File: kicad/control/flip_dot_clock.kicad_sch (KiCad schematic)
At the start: 33 parts, among them U1 NUCLEO-F303K8-HEADER, U10 Small_7_Seg_FlipDot_Module, U2 SLC03B-05, U3 NCV7719, U4 Small_7_Seg_FlipDot_Module, U5 NCV7719, U6 Small_7_Seg_FlipDot_Module, U7 NCV7719, U8 Small_7_Seg_FlipDot_Module, U9 NCV7719

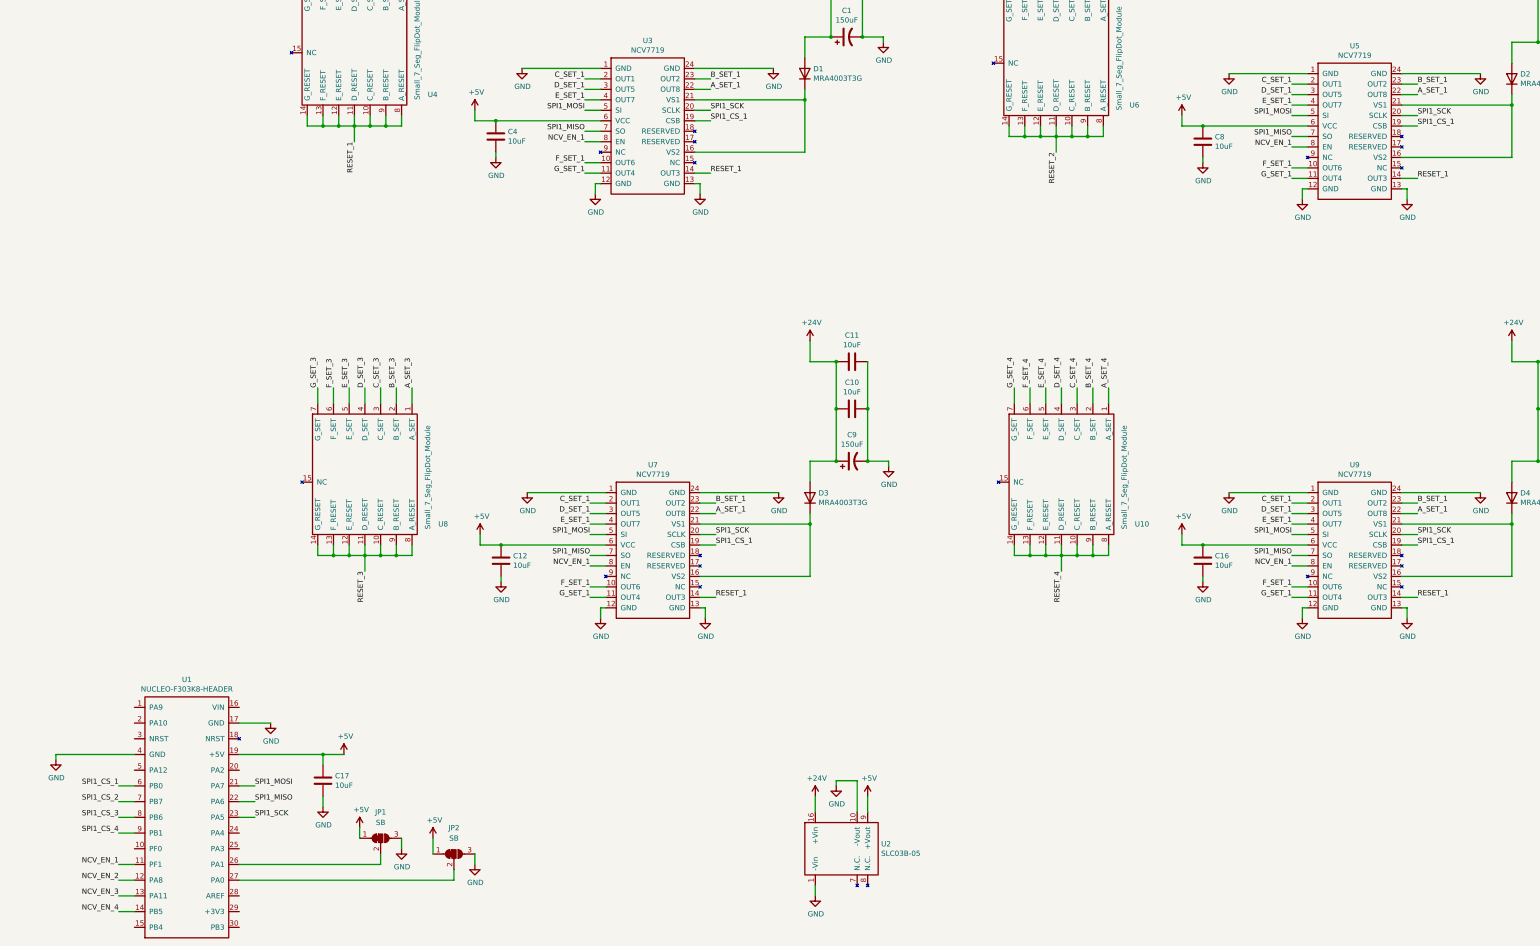
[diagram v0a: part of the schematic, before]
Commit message: all PCB nets connected
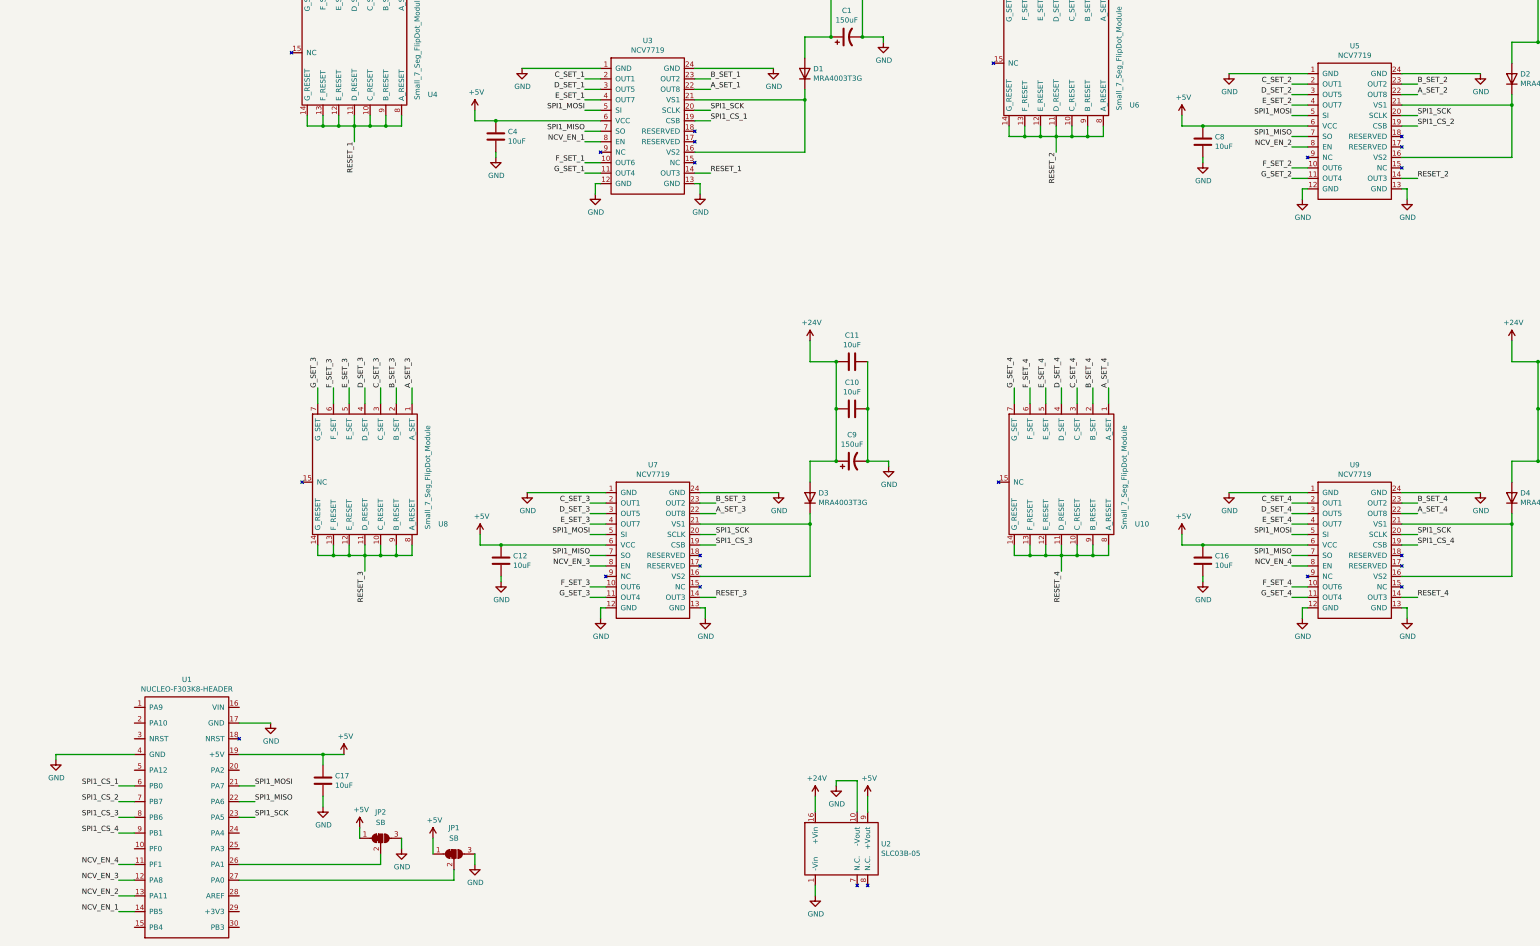
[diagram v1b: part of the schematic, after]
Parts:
- renumbered JP2 to JP1, JP1 to JP2
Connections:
- net A_SET_1: no longer U5.22 (OUT8), U7.22 (OUT8), U9.22 (OUT8)
- net A_SET_2: now also U5.22 (OUT8)
- net A_SET_3: now also U7.22 (OUT8)
- net A_SET_4: now also U9.22 (OUT8)
- net B_SET_1: no longer U5.23 (OUT2), U7.23 (OUT2), U9.23 (OUT2)
- net B_SET_2: now also U5.23 (OUT2)
- net B_SET_3: now also U7.23 (OUT2)
- net B_SET_4: now also U9.23 (OUT2)
- net C_SET_1: no longer U5.2 (OUT1), U7.2 (OUT1), U9.2 (OUT1)
- net C_SET_2: now also U5.2 (OUT1)
- net C_SET_3: now also U7.2 (OUT1)
- net C_SET_4: now also U9.2 (OUT1)
- net D_SET_1: no longer U5.3 (OUT5), U7.3 (OUT5), U9.3 (OUT5)
- net D_SET_2: now also U5.3 (OUT5)
- net D_SET_3: now also U7.3 (OUT5)
- net D_SET_4: now also U9.3 (OUT5)
- net E_SET_1: no longer U5.4 (OUT7), U7.4 (OUT7), U9.4 (OUT7)
- net E_SET_2: now also U5.4 (OUT7)
- net E_SET_3: now also U7.4 (OUT7)
- net E_SET_4: now also U9.4 (OUT7)
- net F_SET_1: no longer U5.10 (OUT6), U7.10 (OUT6), U9.10 (OUT6)
- net F_SET_2: now also U5.10 (OUT6)
- net F_SET_3: now also U7.10 (OUT6)
- net F_SET_4: now also U9.10 (OUT6)
- net G_SET_1: no longer U5.11 (OUT4), U7.11 (OUT4), U9.11 (OUT4)
- net G_SET_2: now also U5.11 (OUT4)
- net G_SET_3: now also U7.11 (OUT4)
- net G_SET_4: now also U9.11 (OUT4)
- net NCV_EN_1: now also U1.14 (PB5); no longer U1.11 (PF1), U5.8 (EN), U7.8 (EN), U9.8 (EN)
- net NCV_EN_2: now also U1.13 (PA11), U5.8 (EN); no longer U1.12 (PA8)
- net NCV_EN_3: now also U1.12 (PA8), U7.8 (EN); no longer U1.13 (PA11)
- net NCV_EN_4: now also U1.11 (PF1), U9.8 (EN); no longer U1.14 (PB5)
- net RESET_1: no longer U5.14 (OUT3), U7.14 (OUT3), U9.14 (OUT3)
- net RESET_2: now also U5.14 (OUT3)
- net RESET_3: now also U7.14 (OUT3)
- net RESET_4: now also U9.14 (OUT3)
- net SPI1_CS_1: no longer U5.19 (CSB), U7.19 (CSB), U9.19 (CSB)
- net SPI1_CS_2: now also U5.19 (CSB)
- net SPI1_CS_3: now also U7.19 (CSB)
- net SPI1_CS_4: now also U9.19 (CSB)

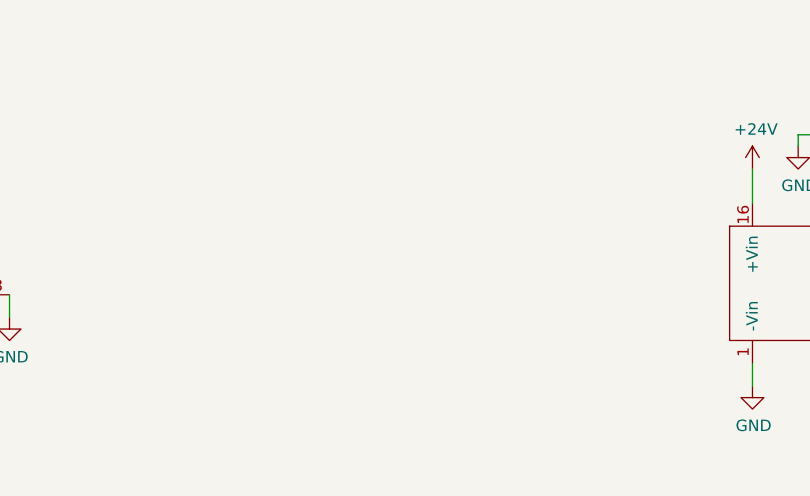
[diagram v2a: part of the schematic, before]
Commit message: update layout, add power connector
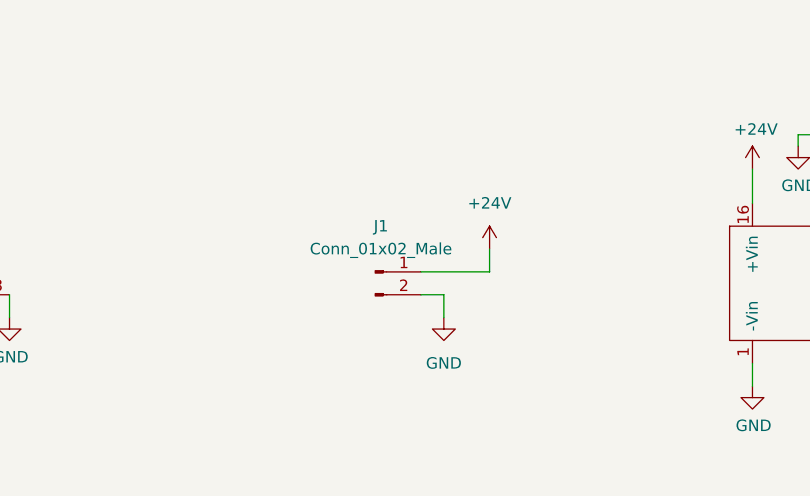
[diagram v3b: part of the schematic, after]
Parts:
- added J1: Conn_01x02_Male, Connector_Molex:Molex_Micro-Fit_3.0_43650-0215_1x02_P3.00mm_Vertical, symbol Connector:Conn_01x02_Male
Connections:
- net +24V: now also J1.1 (Pin_1)
- net GND: now also J1.2 (Pin_2)
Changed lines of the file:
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@@
+    (stroke (width 0) (type default))
+  )
+  (wire (pts (xy 176.53 254) (xy 179.07 254))
     (stroke (width 0) (type default))
   )
@@
     (stroke (width 0) (type default))
   )
+  (wire (pts (xy 184.15 251.46) (xy 184.15 248.92))
+    (stroke (width 0) (type default))
+  )
   (wire (pts (xy 157.48 68.58) (xy 161.29 68.58))
     (stroke (width 0) (type default))
@@
     (stroke (width 0) (type default))
   )
+  (wire (pts (xy 179.07 254) (xy 179.07 256.54))
+    (stroke (width 0) (type default))
+  )
   (wire (pts (xy 158.75 173.99) (xy 162.56 173.99))
     (stroke (width 0) (type default))
@@
   )
   (wire (pts (xy 73.66 241.3) (xy 77.47 241.3))
+    (stroke (width 0) (type default))
+  )
+  (wire (pts (xy 176.53 251.46) (xy 184.15 251.46))
     (stroke (width 0) (type default))
   )
@@
     (pin "2")
   )
+  (symbol (lib_id "power:GND") (at 179.07 256.54 0) (unit 1)
+    (in_bom yes) (on_board yes) (fields_autoplaced)
+    (property "Reference" "#PWR0133" (id 0) (at 179.07 262.89 0)
+      (effects (font (size 1.27 1.27)) hide)
+    )
+    (property "Value" "GND" (id 1) (at 179.07 261.62 0)
+      (effects (font (size 1.27 1.27)))
+    )
+    (property "Footprint" "" (id 2) (at 179.07 256.54 0)
+      (effects (font (size 1.27 1.27)) hide)
+    )
+    (property "Datasheet" "" (id 3) (at 179.07 256.54 0)
+      (effects (font (size 1.27 1.27)) hide)
+    )
+    (pin "1")
+  )
   (symbol (lib_id "power:GND") (at 113.03 252.73 0) (unit 1)
     (in_bom yes) (on_board yes)
@@
     )
     (property "Datasheet" "" (id 3) (at 313.69 166.37 0)
+      (effects (font (size 1.27 1.27)) hide)
+    )
+    (pin "1")
+  )
+  (symbol (lib_id "power:+24V") (at 184.15 248.92 0) (unit 1)
+    (in_bom yes) (on_board yes) (fields_autoplaced)
+    (property "Reference" "#PWR0132" (id 0) (at 184.15 252.73 0)
+      (effects (font (size 1.27 1.27)) hide)
+    )
+    (property "Value" "+24V" (id 1) (at 184.15 243.84 0)
+      (effects (font (size 1.27 1.27)))
+    )
+    (property "Footprint" "" (id 2) (at 184.15 248.92 0)
+      (effects (font (size 1.27 1.27)) hide)
+    )
+    (property "Datasheet" "" (id 3) (at 184.15 248.92 0)
       (effects (font (size 1.27 1.27)) hide)
     )
@@
     (pin "2")
   )
+  (symbol (lib_id "Connector:Conn_01x02_Male") (at 171.45 251.46 0) (unit 1)
+    (in_bom yes) (on_board yes) (fields_autoplaced)
+    (property "Reference" "J1" (id 0) (at 172.085 246.38 0)
+      (effects (font (size 1.27 1.27)))
+    )
+    (property "Value" "Conn_01x02_Male" (id 1) (at 172.085 248.92 0)
+      (effects (font (size 1.27 1.27)))
+    )
+    (property "Footprint" "Connector_Molex:Molex_Micro-Fit_3.0_43650-0215_1x02_P3.00mm_Vertical" (id 2) (at 171.45 251.46 0)
+      (effects (font (size 1.27 1.27)) hide)
+    )
+    (property "Datasheet" "~" (id 3) (at 171.45 251.46 0)
+      (effects (font (size 1.27 1.27)) hide)
+    )
+    (pin "1")
+    (pin "2")
+  )
   (symbol (lib_id "power:GND") (at 356.87 95.25 0) (unit 1)
     (in_bom yes) (on_board yes)
@@
       (reference "#PWR0131") (unit 1) (value "GND") (footprint "")
     )
+    (path "/51440a0f-fda5-409a-af60-703488c8fb65"
+      (reference "#PWR0132") (unit 1) (value "+24V") (footprint "")
+    )
+    (path "/325cf2a4-77b2-46b4-a4a2-ceda54060c78"
+      (reference "#PWR0133") (unit 1) (value "GND") (footprint "")
+    )
     (path "/00000000-0000-0000-0000-000061f1c429"
       (reference "C1") (unit 1) (value "150uF") (footprint "Capacitor_THT:CP_Radial_D10.0mm_P5.00mm")
@@
       (reference "D4") (unit 1) (value "MRA4003T3G") (footprint "Diode_SMD:D_SMA")
     )
+    (path "/d170073c-990e-452b-9e72-8bd3cb8f7a66"
+      (reference "J1") (unit 1) (value "Conn_01x02_Male") (footprint "Connector_Molex:Molex_Micro-Fit_3.0_43650-0215_1x02_P3.00mm_Vertical")
+    )
     (path "/9d9ab09d-0bc7-4056-a994-b66b444cc70c"

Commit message: updates
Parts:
- removed JP1, JP2: SB, Jumper:SolderJumper-3_P2.0mm_Open_TrianglePad1.0x1.5mm_NumberLabels, symbol Jumper:SolderJumper_3_Bridged12
- added JP1, JP2: SJ2O, Jumper:SolderJumper-2_P1.3mm_Open_TrianglePad1.0x1.5mm, symbol Jumper:SolderJumper_2_Open
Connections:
- net +5V: now also JP1.1 (A), JP2.1 (A)
- net at U1.26 (PA1): now also JP2.2 (B)
- net at U1.27 (PA0): now also JP1.2 (B)

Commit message: fix all the kicad files
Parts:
- added J2: Conn_01x15_Female, Connector_PinHeader_2.54mm:PinHeader_1x15_P2.54mm_Vertical, symbol Connector:Conn_01x15_Female
- added J3: Conn_01x03_Male, symbol Connector:Conn_01x03_Male
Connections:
- net +5V: now also J2.10 (Pin_10)
- net GND: now also J2.11 (Pin_11)
- net NCV_EN_1: now also J2.3 (Pin_3)
- net NCV_EN_2: now also J2.15 (Pin_15)
- net NCV_EN_3: now also J2.14 (Pin_14)
- net NCV_EN_4: now also J2.13 (Pin_13)
- net SPI1_CS_1: now also J2.4 (Pin_4)
- net SPI1_CS_2: now also J2.5 (Pin_5)
- net SPI1_CS_3: now also J2.6 (Pin_6)
- net SPI1_CS_4: now also J2.9 (Pin_9)
- net SPI1_MISO: now also J2.12 (Pin_12)
- net SPI1_MOSI: now also J2.7 (Pin_7)
- net SPI1_SCK: now also J2.8 (Pin_8)

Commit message: update pcb
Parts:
- removed J2: Conn_01x15_Female, Connector_PinHeader_2.54mm:PinHeader_1x15_P2.54mm_Vertical, symbol Connector:Conn_01x15_Female
- removed J3: Conn_01x03_Male, symbol Connector:Conn_01x03_Male
- added J2: Conn_02x08_Odd_Even, Connector_PinSocket_2.54mm:PinSocket_2x10_P2.54mm_Vertical, symbol Connector_Generic:Conn_02x10_Odd_Even
- added J3: Conn_01x05_Male, Connector_Molex:Molex_Nano-Fit_105309-xx05_1x05_P2.50mm_Vertical, symbol Connector:Conn_01x05_Male
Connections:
- net GND: now also J3.5 (Pin_5)
- net NCV_EN_1: now also J2.5 (Pin_5)
- net SPI1_CS_1: now also J2.7 (Pin_7)
- net SPI1_CS_2: now also J2.9 (Pin_9)
- net SPI1_CS_3: now also J2.11 (Pin_11)
- net SPI1_CS_4: now also J2.17 (Pin_17)
- net SPI1_MOSI: now also J2.13 (Pin_13)
- net SPI1_SCK: now also J2.15 (Pin_15)
- net HOUR_UP: now reaches U1.1 (PA9)
- net HOUR_UP: now also J2.2 (Pin_2), J3.1 (Pin_1)
- net MIN_DOWN: now reaches U1.15 (PB4)
- net MIN_DOWN: now also J2.4 (Pin_4), J3.4 (Pin_4)
- net HOUR_DOWN: now reaches U1.2 (PA10)
- net HOUR_DOWN: now also J2.1 (Pin_1), J3.2 (Pin_2)
- net MIN_UP: now reaches U1.5 (PA12)
- net MIN_UP: now also J2.3 (Pin_3), J3.3 (Pin_3)
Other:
- moved on the sheet: C1, C13, C5, C9

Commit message: moving along
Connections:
- net +5V: now also J2.6 (Pin_6), J2.8 (Pin_8)
- net GND: now also J2.10 (Pin_10), J2.12 (Pin_12)
- net HOUR_DOWN: now also U1.5 (PA12); no longer U1.2 (PA10)
- net MIN_DOWN: now also U1.2 (PA10); no longer U1.15 (PB4)
- net MIN_UP: now also U1.6 (PB0); no longer U1.5 (PA12)
- net NCV_EN_1: now also U1.7 (PB7); no longer U1.14 (PB5)
- net NCV_EN_2: now also J2.16 (Pin_16)
- net NCV_EN_3: now also J2.18 (Pin_18), U1.14 (PB5); no longer U1.12 (PA8)
- net NCV_EN_4: now also J2.20 (Pin_20), U1.15 (PB4); no longer U1.11 (PF1)
- net SPI1_CS_1: now also U1.24 (PA4); no longer U1.6 (PB0)
- net SPI1_CS_2: now also U1.25 (PA3); no longer U1.7 (PB7)
- net SPI1_CS_3: now also U1.26 (PA1); no longer U1.8 (PB6)
- net SPI1_CS_4: now also U1.27 (PA0); no longer U1.9 (PB1)
- net SPI1_MISO: now also J2.19 (Pin_19)
- net at JP2.2 (B): now also U1.11 (PF1); no longer U1.26 (PA1)
- net at JP1.2 (B): now also U1.12 (PA8); no longer U1.27 (PA0)
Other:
- moved on the sheet: C17, J1, J2, J3, JP1, JP2, U2
